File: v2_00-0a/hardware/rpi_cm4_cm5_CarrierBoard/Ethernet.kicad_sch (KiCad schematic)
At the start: 11 parts, among them J5 0826-1X1T-32-F

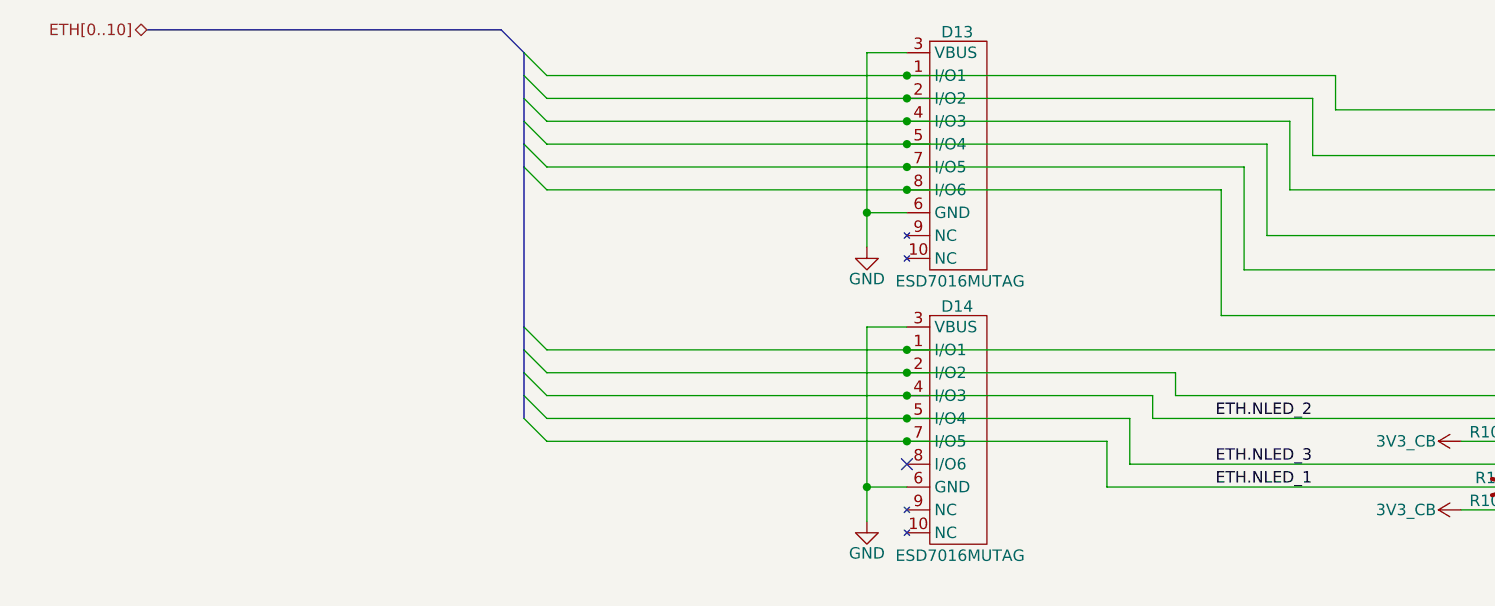
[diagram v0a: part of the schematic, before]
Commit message: Update schematics (several new hierarchical pages, updates bus labels)
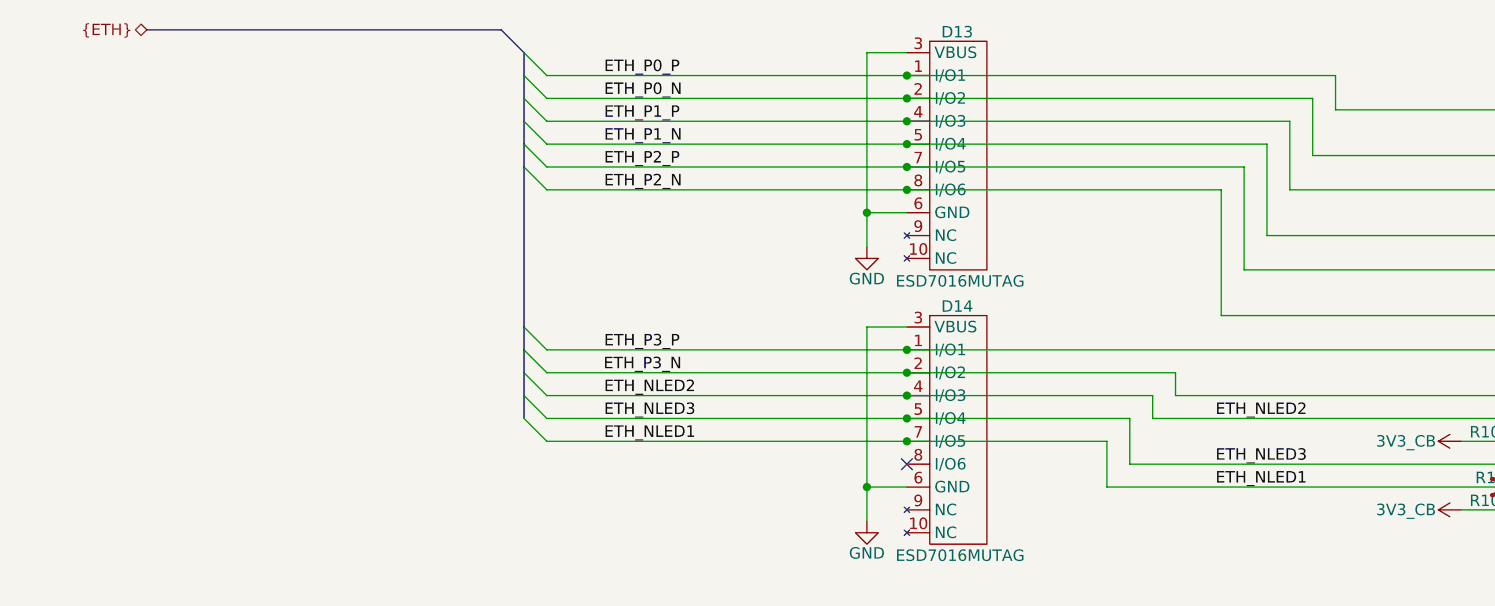
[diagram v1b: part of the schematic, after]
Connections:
- net ETH_P0_N: now reaches D13.2 (I/O2), J5.10 (TRD1-)
- net ETH_P0_P: now reaches D13.1 (I/O1), J5.11 (TRD1+)
- net ETH_P2_N: now reaches D13.8 (I/O6), J5.2 (TRD3-)
- net ETH_P2_P: now reaches D13.7 (I/O5), J5.3 (TRD3+)
- net ETH_P1_P: now reaches D13.4 (I/O3), J5.4 (TRD2+)
- net ETH_P1_N: now reaches D13.5 (I/O4), J5.5 (TRD2-)
- net ETH_P3_P: now reaches D14.1 (I/O1), J5.8 (TRD4+)
- net ETH_P3_N: now reaches D14.2 (I/O2), J5.9 (TRD4-)
- net ETH.NLED_1 renamed ETH_NLED1
- net ETH.NLED_2 renamed ETH_NLED2
- net ETH.NLED_3 renamed ETH_NLED3
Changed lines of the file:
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@@
 		(comment 8 "WIP")
+	)
+	(bus_alias "ETH"
+		(members "ETH_0_P" "ETH_0_N" "ETH_1_P" "ETH_1_N" "ETH_2_P" "ETH_2_N" "ETH_3_P"
+			"ETH_3_N" "ETH_NLED1" "ETH_NLED2" "ETH_NLED3"
+		)
+	)
+	(bus_alias "USB2_HOST"
+		(members "USB_P" "USB_N")
+	)
+	(bus_alias "USB2_OTG"
+		(members "USB_P" "USB_N" "OTG_ID")
+	)
+	(bus_alias "USB3"
+		(members "U3TXD_P" "U3TXD_N" "U3RXD_P" "U3RXD_N" "USB_P" "USB_N" "USB_VBUS")
 	)
 	(junction
@@
 		)
 	)
-	(label "ETH.NLED_3"
+	(label "ETH_P1_N"
+		(at 107.95 69.85 0)
+		(effects
+			(font
+				(size 1.27 1.27)
+			)
+			(justify left bottom)
+		)
+	)
+	(label "ETH_NLED3"
 		(at 175.895 105.41 0)
 		(effects
@@
 		)
 	)
-	(label "ETH.NLED_1"
+	(label "ETH_NLED1"
 		(at 175.895 107.95 0)
 		(effects
@@
 		)
 	)
-	(label "ETH.NLED_2"
+	(label "ETH_P0_N"
+		(at 107.95 64.77 0)
+		(effects
+			(font
+				(size 1.27 1.27)
+			)
+			(justify left bottom)
+		)
+	)
+	(label "ETH_P0_P"
+		(at 107.95 62.23 0)
+		(effects
+			(font
+				(size 1.27 1.27)
+			)
+			(justify left bottom)
+		)
+	)
+	(label "ETH_NLED1"
+		(at 107.95 102.87 0)
+		(effects
+			(font
+				(size 1.27 1.27)
+			)
+			(justify left bottom)
+		)
+	)
+	(label "ETH_P3_N"
+		(at 107.9031 95.25 0)
+		(effects
+			(font
+				(size 1.27 1.27)
+			)
+			(justify left bottom)
+		)
+	)
+	(label "ETH_P1_P"
+		(at 107.95 67.31 0)
+		(effects
+			(font
+				(size 1.27 1.27)
+			)
+			(justify left bottom)
+		)
+	)
+	(label "ETH_P2_P"
+		(at 107.95 72.39 0)
+		(effects
+			(font
+				(size 1.27 1.27)
+			)
+			(justify left bottom)
+		)
+	)
+	(label "ETH_NLED2"
 		(at 175.895 100.33 0)
 		(effects
@@
 		)
 	)
-	(hierarchical_label "ETH[0..10]"
+	(label "ETH_NLED3"
+		(at 107.95 100.33 0)
+		(effects
+			(font
+				(size 1.27 1.27)
+			)
+			(justify left bottom)
+		)
+	)
+	(label "ETH_P2_N"
+		(at 107.95 74.93 0)
+		(effects
+			(font
+				(size 1.27 1.27)
+			)
+			(justify left bottom)
+		)
+	)
+	(label "ETH_NLED2"
+		(at 107.95 97.79 0)
+		(effects
+			(font
+				(size 1.27 1.27)
+			)
+			(justify left bottom)
+		)
+	)
+	(label "ETH_P3_P"
+		(at 107.95 92.71 0)
+		(effects
+			(font
+				(size 1.27 1.27)
+			)
+			(justify left bottom)
+		)
+	)
+	(hierarchical_label "{ETH}"
 		(shape bidirectional)
 		(at 57.15 57.15 180)

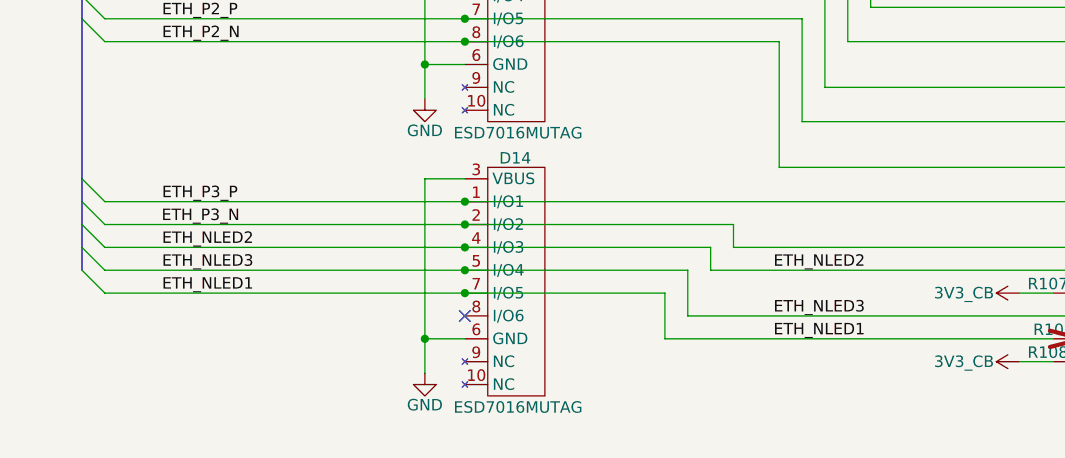
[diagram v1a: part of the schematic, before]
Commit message: Add new page and update schematics
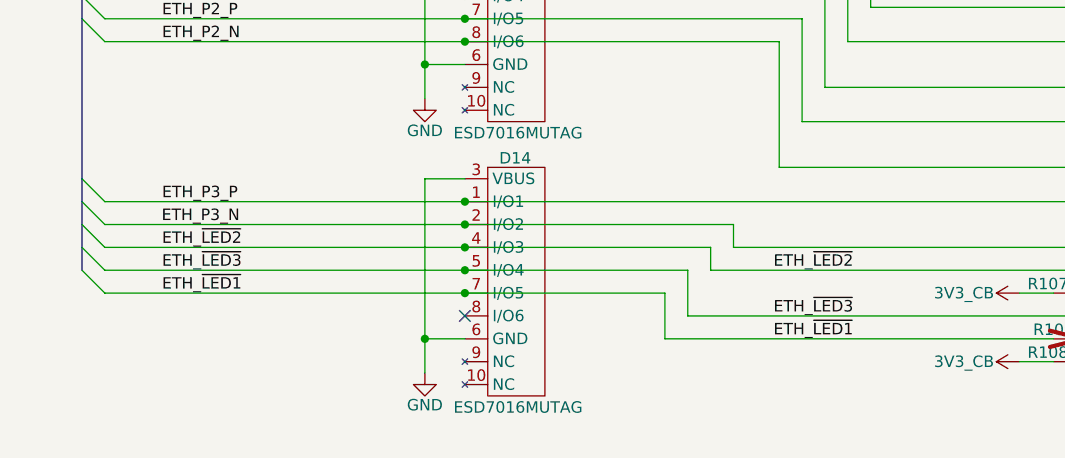
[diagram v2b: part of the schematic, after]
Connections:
- net ETH_NLED1 renamed ETH_~{LED1}
- net ETH_NLED2 renamed ETH_~{LED2}
- net ETH_NLED3 renamed ETH_~{LED3}
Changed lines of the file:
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@@
+		)
+	)
+	(label "ETH_~{LED1}"
+		(at 107.95 102.87 0)
+		(effects
+			(font
+				(size 1.27 1.27)
+			)
+			(justify left bottom)
+		)
+	)
+	(label "ETH_~{LED3}"
+		(at 107.95 100.33 0)
+		(effects
+			(font
+				(size 1.27 1.27)
+			)
+			(justify left bottom)
 		)
 	)
@@
 		)
 	)
-	(label "ETH_NLED3"
+	(label "ETH_~{LED3}"
 		(at 175.895 105.41 0)
 		(effects
@@
 		)
 	)
-	(label "ETH_NLED1"
+	(label "ETH_~{LED1}"
 		(at 175.895 107.95 0)
 		(effects
@@
 	(label "ETH_P0_P"
 		(at 107.95 62.23 0)
-		(effects
-			(font
-				(size 1.27 1.27)
-			)
-			(justify left bottom)
-		)
-	)
-	(label "ETH_NLED1"
-		(at 107.95 102.87 0)
 		(effects
 			(font
@@
 		)
 	)
-	(label "ETH_NLED2"
+	(label "ETH_~{LED2}"
 		(at 175.895 100.33 0)
-		(effects
-			(font
-				(size 1.27 1.27)
-			)
-			(justify left bottom)
-		)
-	)
-	(label "ETH_NLED3"
-		(at 107.95 100.33 0)
 		(effects
 			(font
@@
 		)
 	)
-	(label "ETH_NLED2"
+	(label "ETH_~{LED2}"
 		(at 107.95 97.79 0)
 		(effects

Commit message: Add and modify existing schematics
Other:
- note added: "Resistors are 1% 1/16W 0402 unless otherwise noted Capacitors are 10% 50V X7R 0402 unless otherwise noted"
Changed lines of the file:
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@@
 		(members "U3TXD_P" "U3TXD_N" "U3RXD_P" "U3RXD_N" "USB_P" "USB_N" "USB_VBUS")
+	)
+	(text "Resistors are 1% 1/16W 0402 unless otherwise noted\nCapacitors are 10% 50V X7R 0402 unless otherwise noted"
+		(exclude_from_sim no)
+		(at 12.7 170.942 0)
+		(effects
+			(font
+				(size 1.27 1.27)
+			)
+			(justify left)
+		)
 	)
 	(junction
